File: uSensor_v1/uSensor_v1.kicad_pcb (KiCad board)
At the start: 2 copper layers, 171 x 125 mm, 284 parts, among them J1 +12V Supply, J2 Conn_01x03, J3 Conn_01x03, J4 NS25-W8P 6-pin 2,54mm, J5 USB_B, J6 GNDA-GNDD Jumper, Q1 BC817-25, Q2 BC817-25, Q3 BC847PN-7-F, Q4 BC847PN-7-F, SW1 SW_Push, SW2 SW_Push, U1 AM10TW-2405DZ, U11 AD7795, U12 AD5667, U15 REF192, U2 LD1117A, U22 RCLAMP, U3 STM32F407VGTx, U4 MCP9700AT, U5 MCP9700AT, U6 LM6132A, U7 MCP9700AT, U8 MCP9700AT, U9 UG-2864KSWLG01

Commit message: Layout in progress.
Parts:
- moved U15 263.9 mm to (195.7, 30.6), turned to 90 degrees
- moved C47 263.7 mm to (195.6, 26.8), turned to 180 degrees
- moved C7 259.8 mm to (26.3, 90.0), turned to 90 degrees
- moved C20 257.9 mm to (28.0, 90.0), turned to 90 degrees
- moved C6 247.4 mm to (37.9, 90.0), turned to 90 degrees
- moved TP40 242.0 mm to (180.2, 21.9), turned to 90 degrees
- moved C67 240.2 mm to (21.5, 106.0), turned to 180 degrees
- moved J2 238.2 mm to (177.4, 19.2), turned to 0 degrees
- moved C8 237.6 mm to (21.5, 107.7), turned to 180 degrees
- moved TP71 234.1 mm to (174.3, 16.4), turned to 90 degrees
- moved R13 233.8 mm to (174.3, 19.6), turned to 90 degrees
- moved RV1 233.6 mm to (174.3, 31.6), turned to 90 degrees
- moved R12 233.6 mm to (174.3, 24.1), turned to 90 degrees
- moved U3 233.5 mm to (32.9, 101.4), turned to 180 degrees
- moved Q1 229.4 mm to (171.2, 20.1), turned to 270 degrees
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
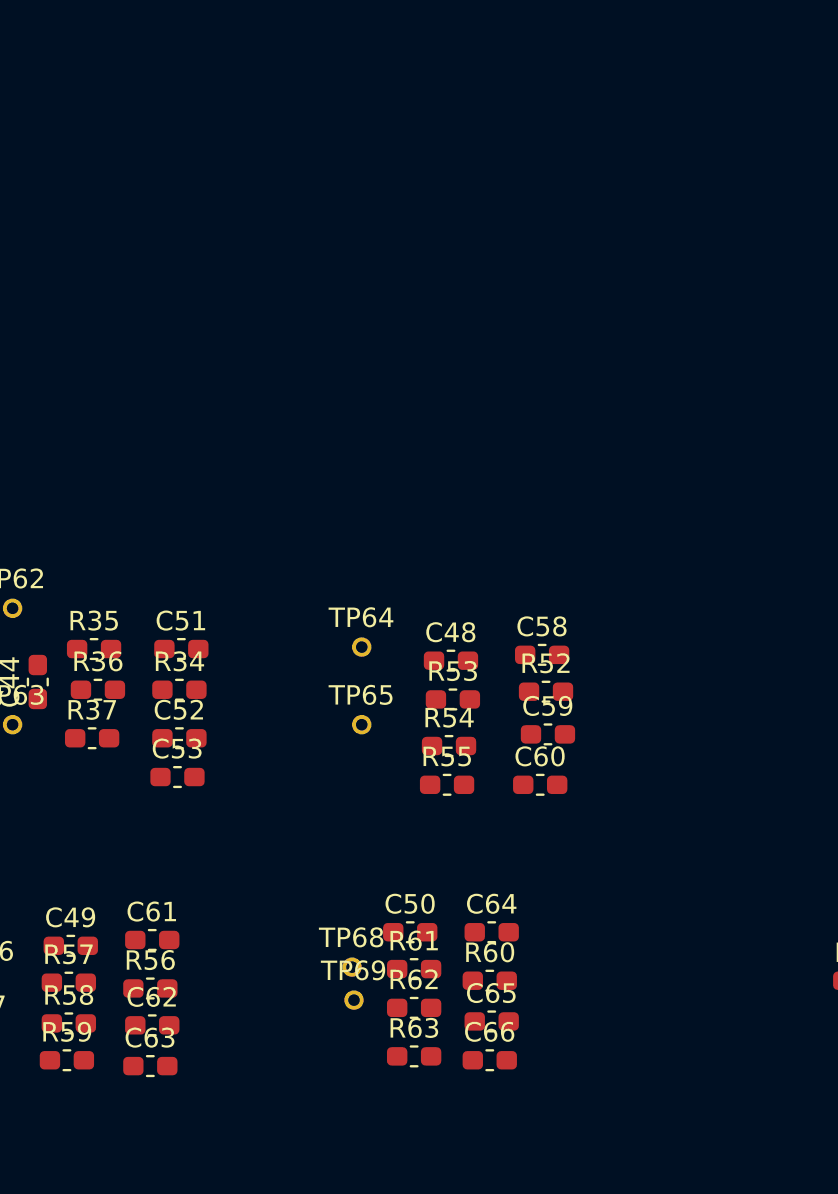
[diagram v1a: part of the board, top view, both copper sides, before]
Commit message: Schematic changed (added 2channel opamp in one HS)
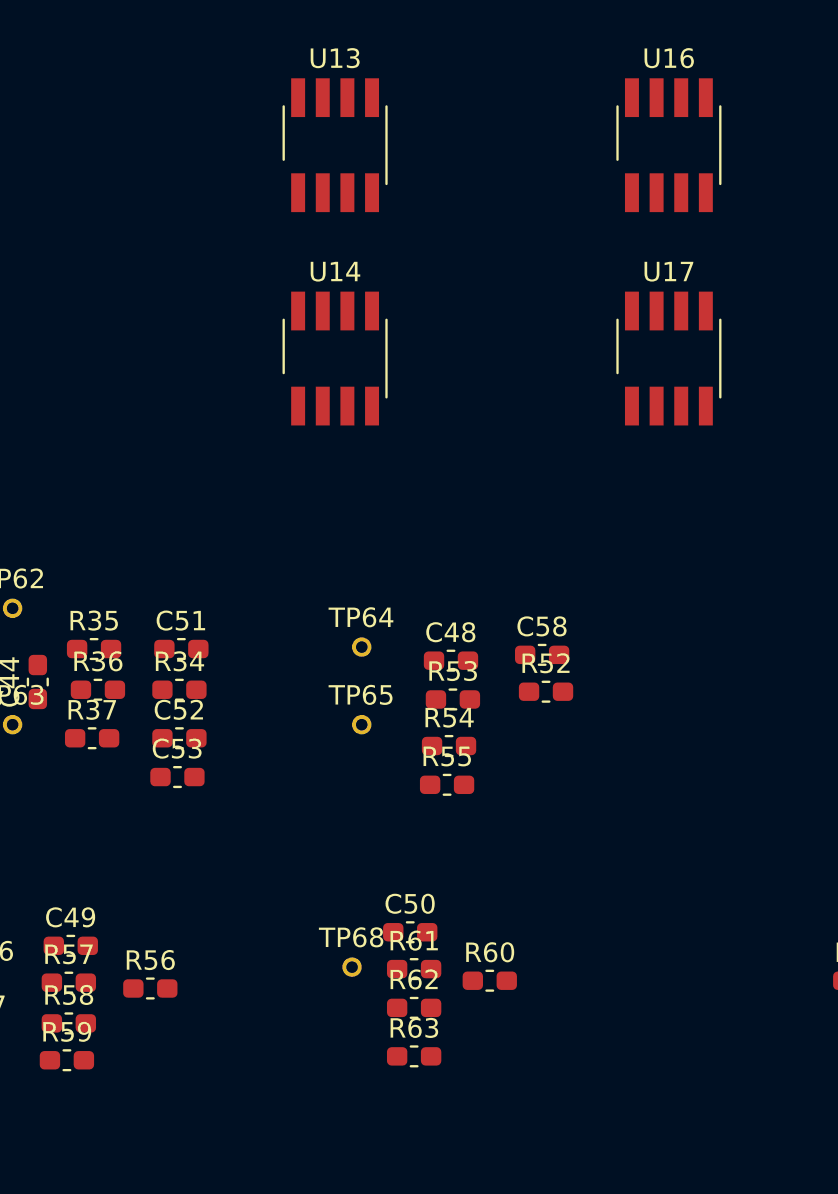
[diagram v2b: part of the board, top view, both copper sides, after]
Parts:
- removed C59, C60, C62, C63, C65, C66: 100n 6V3 X5R, Capacitor_SMD:C_0603_1608Metric_Pad1.05x0.95mm_HandSolder
- removed C61, C64: 1p 16V X5R, Capacitor_SMD:C_0603_1608Metric_Pad1.05x0.95mm_HandSolder
- removed TP69: TP, Sentisa-Connectors:TestPoint_Probe_1.0mmDiameter_0.6mmDrill
- added U13: TBD, Sentisa-IC:SO-8, F.Cu at (106.0, -53.4)
- added U14: TBD, Sentisa-IC:SO-8, F.Cu at (106.0, -42.4)
- added U16: TBD, Sentisa-IC:SO-8, F.Cu at (123.2, -53.4)
- added U17: TBD, Sentisa-IC:SO-8, F.Cu at (123.2, -42.4)
- C49, C50: value 10n 6V3 X5R -> 1p 16V X5R
- C51, C58: value 1p 16V X5R -> 100n 6V3 X5R
- C53, C55: value 100n 6V3 X5R -> 1p 16V X5R
- R35, R54, R57, R62: value 10k 1% -> 22k 1%
- R37, R52, R59, R60: value 22k 1% -> 10k 1%
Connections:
- C49 pad 1: REF_2.5V -> /SENS_IN_AMP_CH_A_B/SENS_OUT_1
- C49 pad 2: GNDA -> Net-(C49-Pad2)
- C50 pad 1: REF_2.5V -> /SENS_IN_AMP_CH_A_B/SENS_OUT_2
- C50 pad 2: GNDA -> Net-(C50-Pad2)
- C51 pad 1: /SENS_IN_AMP_A/SENS_OUT -> +5V
- C51 pad 2: Net-(C51-Pad2) -> GNDA
- C52 pad 1: +5V -> -5V
- C53 pad 1: -5V -> /SENS_IN_AMP_CH_C_D/SENS_OUT_1
- C53 pad 2: GNDA -> Net-(C53-Pad2)
- C55 pad 1: -5V -> /SENS_IN_AMP_CH_C_D/SENS_OUT_2
- C55 pad 2: GNDA -> Net-(C55-Pad2)
- C58 pad 1: /SENS_IN_AMP_B/SENS_OUT -> -5V
- C58 pad 2: Net-(C58-Pad2) -> GNDA
- R27 pad 2: /SENS_IN_AMP_B/SENS_OUT -> /SENS_IN_AMP_CH_A_B/SENS_OUT_2
- R28 pad 2: /SENS_IN_AMP_D/SENS_OUT -> /SENS_IN_AMP_CH_C_D/SENS_OUT_2
- R30 pad 2: /SENS_IN_AMP_A/SENS_OUT -> /SENS_IN_AMP_CH_A_B/SENS_OUT_1
- R32 pad 2: /SENS_IN_AMP_C/SENS_OUT -> /SENS_IN_AMP_CH_C_D/SENS_OUT_1
- R34 pad 1: /SENS_IN_AMP_A/SENS_OUT -> /SENS_IN_AMP_CH_A_B/SENS_OUT_1
- R34 pad 2: Net-(C51-Pad2) -> Net-(C49-Pad2)
- R35 pad 1: Net-(C51-Pad2) -> /SENS_IN_AMP_CH_A_B/SENS_OUT_2
- R35 pad 2: SENS_A -> Net-(C50-Pad2)
- R36 pad 1: Net-(R36-Pad1) -> Net-(C49-Pad2)
- R36 pad 2: REF_2.5V -> SENS_A
- R37 pad 1: GNDA -> Net-(C50-Pad2)
- R37 pad 2: Net-(R36-Pad1) -> SENS_B
- R52 pad 1: /SENS_IN_AMP_B/SENS_OUT -> Net-(R52-Pad1)
- R52 pad 2: Net-(C58-Pad2) -> REF_2.5V
- R53 pad 1: Net-(C58-Pad2) -> Net-(R53-Pad1)
- R53 pad 2: SENS_B -> REF_2.5V
- R54 pad 1: Net-(R54-Pad1) -> GNDA
- R54 pad 2: REF_2.5V -> Net-(R52-Pad1)
- R55 pad 2: Net-(R54-Pad1) -> Net-(R53-Pad1)
- R56 pad 1: /SENS_IN_AMP_C/SENS_OUT -> /SENS_IN_AMP_CH_C_D/SENS_OUT_1
- R56 pad 2: Net-(C61-Pad2) -> Net-(C53-Pad2)
- R57 pad 1: Net-(C61-Pad2) -> /SENS_IN_AMP_CH_C_D/SENS_OUT_2
- R57 pad 2: SENS_C -> Net-(C55-Pad2)
- R58 pad 1: Net-(R58-Pad1) -> Net-(C53-Pad2)
- R58 pad 2: REF_2.5V -> SENS_C
- R59 pad 1: GNDA -> Net-(C55-Pad2)
- R59 pad 2: Net-(R58-Pad1) -> SENS_D
- R60 pad 1: /SENS_IN_AMP_D/SENS_OUT -> Net-(R60-Pad1)
- R60 pad 2: Net-(C64-Pad2) -> REF_2.5V
- R61 pad 1: Net-(C64-Pad2) -> Net-(R61-Pad1)
- R61 pad 2: SENS_D -> REF_2.5V
- R62 pad 1: Net-(R62-Pad1) -> GNDA
- R62 pad 2: REF_2.5V -> Net-(R60-Pad1)
- R63 pad 2: Net-(R62-Pad1) -> Net-(R61-Pad1)
- TP52 pad 1: /SENS_IN_AMP_A/SENS_OUT -> /SENS_IN_AMP_CH_A_B/SENS_OUT_1
- TP56 pad 1: /SENS_IN_AMP_B/SENS_OUT -> /SENS_IN_AMP_CH_A_B/SENS_OUT_2
- TP57 pad 1: /SENS_IN_AMP_D/SENS_OUT -> /SENS_IN_AMP_CH_C_D/SENS_OUT_2
- TP60 pad 1: /SENS_IN_AMP_C/SENS_OUT -> /SENS_IN_AMP_CH_C_D/SENS_OUT_1
- TP61 pad 1: /SENS_IN_AMP_D/SENS_OUT -> Net-(C49-Pad2)
- TP62 pad 1: Net-(C51-Pad2) -> Net-(C50-Pad2)
- TP63 pad 1: Net-(R36-Pad1) -> Net-(R52-Pad1)
- TP64 pad 1: Net-(C58-Pad2) -> Net-(R53-Pad1)
- TP65 pad 1: Net-(R54-Pad1) -> Net-(C53-Pad2)
- TP66 pad 1: Net-(C61-Pad2) -> Net-(C55-Pad2)
- TP67 pad 1: Net-(R58-Pad1) -> Net-(R60-Pad1)
- TP68 pad 1: Net-(C64-Pad2) -> Net-(R61-Pad1)

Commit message: Layout in progress.
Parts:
- added C59: 10n 6V3 X5R, Capacitor_SMD:C_0603_1608Metric_Pad1.05x0.95mm_HandSolder, F.Cu at (-38.9, 78.1)
- added C60: 10n 6V3 X5R, Capacitor_SMD:C_0603_1608Metric_Pad1.05x0.95mm_HandSolder, F.Cu at (-26.3, 78.1)
- added J7: Barrel_Jack_Switch, Connector_BarrelJack:BarrelJack_Wuerth_6941xx301002, F.Cu at (26.6, 17.5)
- added U10: KSS-213 Connector, Connector_FFC-FPC:TE_1-84952-6_1x16-1MP_P1.0mm_Horizontal, F.Cu at (55.8, -37.7)
- moved TP61 218.2 mm to (-43.6, 58.8)
- moved U17 194.3 mm to (-32.6, 73.7), turned to 270 degrees
- moved U16 192.8 mm to (-32.9, 59.7), turned to 270 degrees
- moved C58 183.6 mm to (-34.2, 77.5)
- moved R52 179.3 mm to (-40.1, 61.5), turned to 270 degrees
- moved TP65 178.8 mm to (-43.3, 72.8)
- moved R60 176.1 mm to (-39.8, 75.5), turned to 270 degrees
- moved R54 172.1 mm to (-38.4, 61.5), turned to 90 degrees
- moved R62 170.5 mm to (-38.1, 75.5), turned to 90 degrees
- moved C53 166.0 mm to (-39.8, 71.9), turned to 270 degrees
- moved C48 165.7 mm to (-26.6, 64.1)
- moved R53 164.0 mm to (-27.4, 61.5), turned to 270 degrees
- moved R61 160.7 mm to (-25.4, 75.5), turned to 270 degrees
- moved R55 160.0 mm to (-25.7, 61.5), turned to 90 degrees
- moved R63 159.8 mm to (-27.1, 75.5), turned to 90 degrees
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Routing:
- net Net-(C11-Pad2): track 0.00 -> 48.6 mm
- net +3V3: track 0.00 -> 33.2 mm
- net Net-(C12-Pad1): track 0.00 -> 17.0 mm
- net +5V: track 0.00 -> 16.9 mm
- net -5V: track 0.00 -> 16.5 mm
- net Net-(C11-Pad1): track 0.00 -> 14.6 mm
- net Net-(D1-Pad2): track 0.00 -> 14.2 mm
- net Net-(C14-Pad2): track 0.00 -> 10.2 mm
- net Net-(C9-Pad1): track 0.00 -> 9.95 mm
- net Net-(C50-Pad2): track 0.00 -> 8.91 mm
- net Net-(C55-Pad2): track 0.00 -> 8.91 mm
- net Net-(C49-Pad2): track 0.00 -> 8.38 mm
- net Net-(C53-Pad2): track 0.00 -> 8.38 mm
- net Net-(R9-Pad1): track 0.00 -> 7.00 mm
- net Net-(R10-Pad1): track 0.00 -> 7.00 mm
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
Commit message: Layout in progress.
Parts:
- moved RV1 281.4 mm to (-104.7, 68.1), turned to 0 degrees
- moved TP77 277.6 mm to (-116.0, 61.4)
- moved J3 275.6 mm to (-118.8, 64.2), turned to 90 degrees
- moved TP73 275.0 mm to (-113.7, 67.0)
- moved R2 274.3 mm to (-114.3, 60.5), turned to 90 degrees
- moved R1 272.8 mm to (-112.6, 60.5), turned to 90 degrees
- moved C19 272.3 mm to (-103.8, 58.3)
- moved U6 272.2 mm to (-105.4, 62.3)
- moved C1 271.9 mm to (-99.9, 59.8)
- moved R3 271.3 mm to (-110.9, 60.5), turned to 270 degrees
- moved R5 271.2 mm to (-110.9, 64.1), turned to 270 degrees
- moved TP76 270.4 mm to (-98.2, 58.9)
- moved TP75 270.3 mm to (-110.9, 57.9)
- moved TP74 267.9 mm to (-98.6, 66.0)
- moved R4 265.7 mm to (-99.9, 63.4), turned to 90 degrees
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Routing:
- net Net-(RV1-Pad2): track 0.00 -> 12.0 mm
- net Net-(R26-Pad1): track 0.00 -> 8.42 mm
- net Net-(R1-Pad1): track 0.00 -> 8.28 mm
- net Net-(R26-Pad2): track 0.00 -> 7.82 mm, vias 0 -> 2
- net Net-(C43-Pad2): track 0.00 -> 6.87 mm
- net Net-(C1-Pad1): track 0.00 -> 6.78 mm
- net Net-(C1-Pad2): track 0.00 -> 6.78 mm
- net Net-(R27-Pad1): track 0.00 -> 6.71 mm
- net Net-(J3-Pad3): track 0.00 -> 6.39 mm
- net Net-(R31-Pad1): track 0.00 -> 6.15 mm
- net Net-(R3-Pad1): track 0.00 -> 5.09 mm
- net +5V: track 16.9 -> 21.2 mm
- net -5V: track 16.5 -> 18.4 mm
- net /SENS_IN_AMP_CH_C_D/SENS_OUT_1: track 5.07 -> 6.89 mm
- net /SENS_IN_AMP_CH_C_D/SENS_OUT_2: track 6.30 -> 8.02 mm
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
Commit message: Layout in progress.
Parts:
- added R75: 100k, Resistor_SMD:R_0603_1608Metric_Pad1.05x0.95mm_HandSolder, F.Cu at (36.4, -23.6)
- added SW3: SW_Push, Button_Switch_THT:SW_PUSH_6mm_H4.3mm, F.Cu at (26.7, -22.9)
- U10: footprint Connector_FFC-FPC:TE_1-84952-6_1x16-1MP_P1.0mm_Horizontal -> Sentisa-Connectors:Molex_52271-1679_1x16_1mm_Pitch_FFC_FPC_Horizontal_SMT
- moved J3 265.3 mm to (145.7, 84.7), turned to 180 degrees
- moved TP73 262.5 mm to (148.5, 79.6), turned to 180 degrees
- moved TP77 259.7 mm to (142.9, 81.9), turned to 180 degrees
- moved R2 257.1 mm to (142.0, 80.2), turned to 180 degrees
- moved R5 256.8 mm to (145.6, 76.8), turned to 0 degrees
- moved R1 255.2 mm to (142.0, 78.5), turned to 180 degrees
- moved RV1 254.3 mm to (149.6, 70.6), turned to 270 degrees
- moved R3 253.4 mm to (142.0, 76.8), turned to 0 degrees
- moved TP75 251.0 mm to (139.4, 76.8), turned to 180 degrees
- moved U6 249.4 mm to (143.8, 71.3), turned to 0 degrees
- moved TP74 246.1 mm to (147.5, 64.5), turned to 180 degrees
- moved R4 244.8 mm to (144.9, 65.8), turned to 180 degrees
- moved C19 243.9 mm to (139.8, 69.7), turned to 270 degrees
- moved TP78 242.2 mm to (144.0, 64.1), turned to 180 degrees
- moved C1 241.3 mm to (141.3, 65.8), turned to 0 degrees
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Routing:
- net REF_2.5V: track 6.96 -> 113.2 mm
- net +5V: track 21.2 -> 57.7 mm
- net COIL_F+: track 0.00 -> 20.4 mm
- net COIL_T-: track 0.00 -> 19.1 mm
- net /SENS_IN_AMP_CH_A_B/SENS_OUT_2: track 7.96 -> 25.4 mm
- net /SENS_IN_AMP_CH_C_D/SENS_OUT_1: track 6.89 -> 23.6 mm, vias 0 -> 1
- net Net-(R39-Pad2): track 0.00 -> 14.0 mm
- net SENS_LD: track 0.00 -> 13.3 mm
- net COIL_T+: track 0.00 -> 13.0 mm
- net COIL_F-: track 0.00 -> 12.6 mm
- net Net-(R46-Pad2): track 0.00 -> 11.3 mm
- net Net-(TP45-Pad1): track 0.00 -> 10.4 mm
- net SENS_C: track 0.00 -> 9.51 mm
- net Net-(TP34-Pad1): track 0.00 -> 9.19 mm
- net Net-(Q4-Pad2): track 0.00 -> 9.06 mm, vias 0 -> 2
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- added copper zone on F.Cu, net GNDA
- added copper zone on F.Cu, net GNDD
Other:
- rule pad_to_mask_clearance: 0.051 -> 0.1
- rule solder_mask_min_width: 0.25 -> 0.05

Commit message: Layout in progress.
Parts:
- moved TP1 308.1 mm to (231.3, 117.3)
- moved TP10 308.1 mm to (223.2, 126.3)
- moved TP11 308.1 mm to (230.4, 130.5)
- moved TP13 308.1 mm to (236.3, 114.3)
- moved TP14 308.1 mm to (228.1, 121.7)
- moved TP15 308.1 mm to (226.5, 123.3)
- moved TP17 308.1 mm to (231.2, 118.9)
- moved TP18 308.1 mm to (247.1, 124.4)
- moved TP19 308.1 mm to (243.3, 128.8)
- moved TP2 308.1 mm to (221.9, 114.8)
- moved TP20 308.1 mm to (234.4, 127.5)
- moved TP24 308.1 mm to (226.5, 121.7)
- moved TP25 308.1 mm to (230.4, 132.1)
- moved TP28 308.1 mm to (220.7, 131.3)
- moved TP29 308.1 mm to (234.7, 115.8)
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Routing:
- net Net-(J5-Pad3): track 0.00 -> 10.3 mm
- net Net-(R23-Pad1): track 0.00 -> 9.27 mm
- net Net-(R21-Pad1): track 0.00 -> 9.27 mm
- net USB_VBUS: track 0.00 -> 7.17 mm
- net Net-(J4-Pad6): track 0.00 -> 7.06 mm
- net Net-(J4-Pad5): track 0.00 -> 6.60 mm
- net Net-(J4-Pad2): track 0.00 -> 5.79 mm
- net Net-(J4-Pad4): track 0.00 -> 5.78 mm
- net PROG_SWCLK: track 0.00 -> 4.61 mm
- net Net-(J5-Pad2): track 0.00 -> 4.03 mm
- net USB_D-: track 0.00 -> 3.94 mm, vias 0 -> 1
- net USB_D+: track 0.00 -> 3.89 mm, vias 0 -> 1
- net PROG_SWDIO: track 0.00 -> 3.74 mm
- net SWITCH_2: track 0.00 -> 3.55 mm
- net SWITCH_1: track 0.00 -> 3.55 mm
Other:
- board size 171 x 125 mm -> 171 x 86.1 mm

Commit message: Layout in progress.
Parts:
- moved TP6 172.6 mm to (69.1, 78.8)
- moved TP11 166.9 mm to (71.1, 80.8)
- moved TP14 160.8 mm to (73.1, 78.8)
- moved TP10 159.3 mm to (71.1, 78.8)
- moved TP7 158.2 mm to (69.1, 80.8)
- moved J6 101.3 mm to (117.7, 55.4), turned to 0 degrees
- moved C70 92.8 mm to (123.3, 45.7), turned to 180 degrees
- moved R70 92.1 mm to (123.3, 47.5), turned to 0 degrees
- moved R72 91.9 mm to (122.6, 62.3), turned to 0 degrees
- moved C31 91.8 mm to (122.5, 54.0), turned to 180 degrees
- moved C34 91.7 mm to (122.5, 59.7), turned to 180 degrees
- moved C69 91.3 mm to (123.3, 49.3), turned to 180 degrees
- moved R69 90.8 mm to (123.3, 51.1), turned to 0 degrees
- moved C32 90.0 mm to (123.3, 56.0), turned to 180 degrees
- moved C33 90.0 mm to (123.3, 57.7), turned to 180 degrees
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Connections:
- R68 pad 1: SENS_B -> SENS_D
- R69 pad 1: SENS_C -> SENS_PD
- R70 pad 1: SENS_D -> FOC_ERR_2_ADC
- R73 pad 1: FOC_ERR_2_ADC -> SENS_B
- R74 pad 1: SENS_PD -> SENS_C
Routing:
- net SWITCH_1: track 3.55 -> 79.9 mm
- net LCD_RST: track 0.00 -> 70.5 mm, vias 0 -> 2
- net LCD_CS: track 0.00 -> 68.8 mm, vias 0 -> 2
- net LCD_A0: track 0.00 -> 67.2 mm, vias 0 -> 2
- net LCD_SCK: track 0.00 -> 65.4 mm, vias 0 -> 2
- net LCD_SI: track 0.00 -> 64.0 mm, vias 0 -> 2
- net +3V3: track 33.2 -> 87.5 mm, vias 0 -> 1
- net PROG_~RST: track 0.00 -> 49.3 mm, vias 0 -> 5
- net SENS_D: track 8.26 -> 32.9 mm
- net SENS_A: track 8.02 -> 32.6 mm
- net SENS_B: track 8.48 -> 32.8 mm
- net SENS_C: track 9.51 -> 33.2 mm
- net USB_VBUS: track 7.17 -> 30.5 mm, vias 0 -> 1
- net USB_D-: track 3.94 -> 24.3 mm, vias 1 -> 2
- net USB_D+: track 3.89 -> 24.2 mm, vias 1 -> 2
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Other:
- board size 171 x 86.1 mm -> 171 x 76.4 mm

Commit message: Layout in progress.
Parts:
- moved TP42 128.9 mm to (139.7, 25.9)
- moved TP41 125.6 mm to (162.4, 23.7)
- moved TP44 105.6 mm to (167.9, 35.2)
- moved C31 20.0 mm to (141.9, 49.0)
- moved C34 20.0 mm to (141.9, 54.7)
- moved C46 20.0 mm to (155.9, 45.9)
- moved C68 20.0 mm to (155.9, 42.3)
- moved C71 20.0 mm to (155.9, 49.5)
- moved C72 20.0 mm to (155.9, 53.1)
- moved R67 20.0 mm to (155.9, 47.7)
- moved R68 20.0 mm to (155.9, 44.1)
- moved R72 20.0 mm to (142.0, 57.3)
- moved R73 20.0 mm to (155.9, 51.3)
- moved R74 20.0 mm to (155.9, 54.9)
- moved TP46 20.0 mm to (149.3, 55.8)
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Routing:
- net SENS_B: track 32.8 -> 55.8 mm, vias 0 -> 1
- net SENS_C: track 33.2 -> 22.6 mm, vias 0 -> 1
- net REF_2.5V: track 113.2 -> 121.9 mm
- net SENS_A: track 32.6 -> 39.7 mm, vias 0 -> 1
- net COIL_F-: track 12.6 -> 16.6 mm
- net COIL_T-: track 19.1 -> 22.8 mm
- net SENS_LD: track 13.3 -> 16.2 mm
- net SENS_D: track 32.9 -> 35.5 mm, vias 0 -> 1
- net Net-(TP45-Pad1): track 10.4 -> 13.0 mm
- net Net-(TP34-Pad1): track 9.19 -> 11.4 mm
- net COIL_T+: track 13.0 -> 15.1 mm
- net COIL_F+: track 20.4 -> 22.1 mm
- net Net-(C49-Pad2): track 8.38 -> 9.84 mm
